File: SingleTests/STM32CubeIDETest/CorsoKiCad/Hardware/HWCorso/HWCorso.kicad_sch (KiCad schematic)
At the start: 9 parts

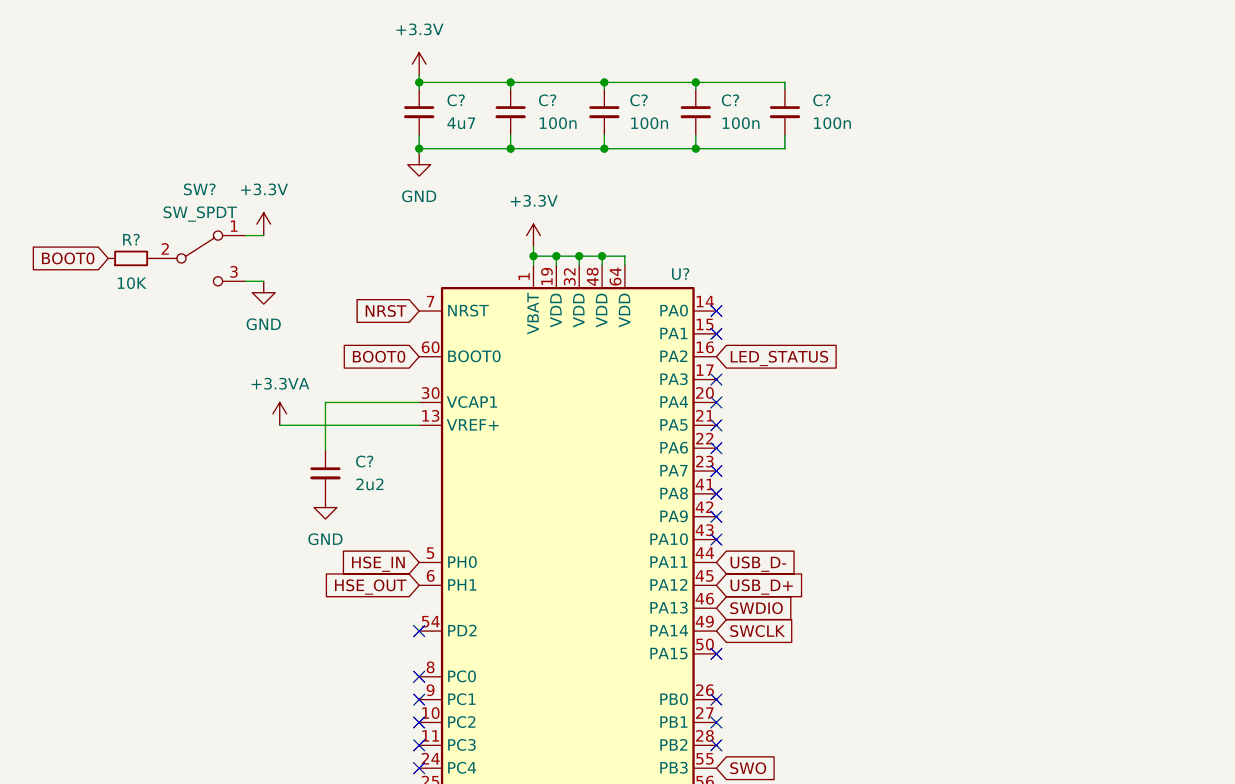
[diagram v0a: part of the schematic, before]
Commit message: Aggiunta dei filtri negli input e Cristallo
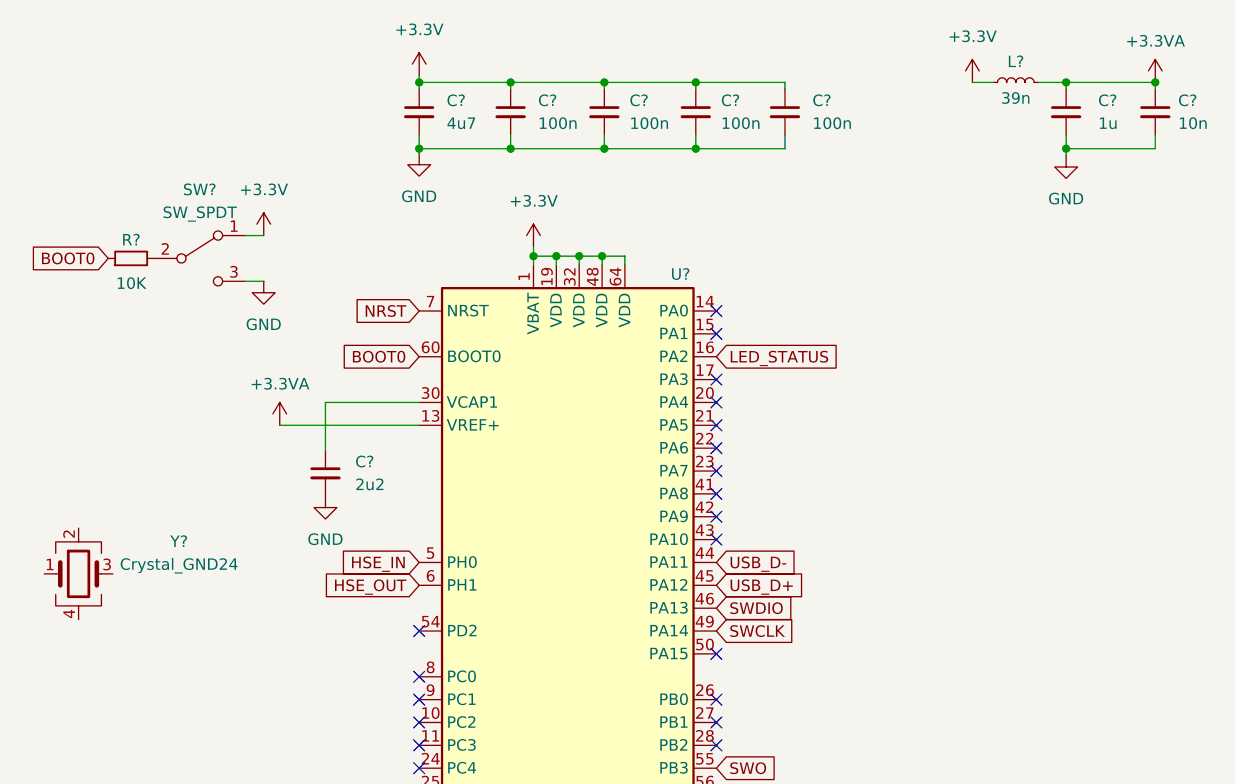
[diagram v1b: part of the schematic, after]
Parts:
- added C?: 10n, symbol Device:C_Small
- added C?: 1u, symbol Device:C_Small
- added L?: 39n, symbol Device:L_Small
- added Y?: Crystal_GND24, symbol Device:Crystal_GND24
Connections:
- net +3.3VA: now also C?.1, C?.1, L?.2
- net +3V3: now also L?.1
- net GND: now also C?.2, C?.2
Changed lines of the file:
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@@
     (company "Giovanni Rasera")
   )
+  (junction (at 133.604 71.882) (diameter 0) (color 0 0 0 0)
+  )
   (junction (at 92.456 71.882) (diameter 0) (color 0 0 0 0)
   )
+  (junction (at 133.604 79.248) (diameter 0) (color 0 0 0 0)
+  )
   (junction (at 82.296 71.882) (diameter 0) (color 0 0 0 0)
+  )
+  (junction (at 143.51 71.882) (diameter 0) (color 0 0 0 0)
   )
   (junction (at 71.882 79.248) (diameter 0) (color 0 0 0 0)
@@
     (stroke (width 0) (type default) (color 0 0 0 0))
   )
+  (wire (pts (xy 133.604 79.248) (xy 133.604 80.01))
+    (stroke (width 0) (type default) (color 0 0 0 0))
+  )
   (wire (pts (xy 79.502 181.102) (xy 79.502 182.372))
     (stroke (width 0) (type default) (color 0 0 0 0))
@@
     (stroke (width 0) (type default) (color 0 0 0 0))
   )
+  (wire (pts (xy 130.556 71.882) (xy 133.604 71.882))
+    (stroke (width 0) (type default) (color 0 0 0 0))
+  )
+  (wire (pts (xy 133.604 79.248) (xy 143.51 79.248))
+    (stroke (width 0) (type default) (color 0 0 0 0))
+  )
   (wire (pts (xy 92.456 77.724) (xy 92.456 79.248))
     (stroke (width 0) (type default) (color 0 0 0 0))
@@
     (stroke (width 0) (type default) (color 0 0 0 0))
   )
+  (wire (pts (xy 123.19 71.882) (xy 125.476 71.882))
+    (stroke (width 0) (type default) (color 0 0 0 0))
+  )
   (wire (pts (xy 92.456 72.644) (xy 92.456 71.882))
     (stroke (width 0) (type default) (color 0 0 0 0))
@@
     (stroke (width 0) (type default) (color 0 0 0 0))
   )
+  (wire (pts (xy 143.51 71.882) (xy 133.604 71.882))
+    (stroke (width 0) (type default) (color 0 0 0 0))
+  )
   (wire (pts (xy 71.882 79.248) (xy 71.882 77.724))
     (stroke (width 0) (type default) (color 0 0 0 0))
   )
+  (wire (pts (xy 143.51 79.248) (xy 143.51 77.724))
+    (stroke (width 0) (type default) (color 0 0 0 0))
+  )
   (wire (pts (xy 79.502 91.186) (xy 82.042 91.186))
     (stroke (width 0) (type default) (color 0 0 0 0))
@@
     (stroke (width 0) (type default) (color 0 0 0 0))
   )
+  (wire (pts (xy 133.604 77.724) (xy 133.604 79.248))
+    (stroke (width 0) (type default) (color 0 0 0 0))
+  )
+  (wire (pts (xy 143.51 72.644) (xy 143.51 71.882))
+    (stroke (width 0) (type default) (color 0 0 0 0))
+  )
   (wire (pts (xy 74.422 181.102) (xy 74.422 182.372))
     (stroke (width 0) (type default) (color 0 0 0 0))
@@
   )
   (wire (pts (xy 61.722 79.248) (xy 61.722 79.756))
+    (stroke (width 0) (type default) (color 0 0 0 0))
+  )
+  (wire (pts (xy 133.604 71.882) (xy 133.604 72.644))
     (stroke (width 0) (type default) (color 0 0 0 0))
   )
@@
       (effects (font (size 1.27 1.27)) (justify right) hide)
     )
+  )
+  (symbol (lib_id "Device:L_Small") (at 128.016 71.882 90) (unit 1)
+    (in_bom yes) (on_board yes)
+    (property "Reference" "L?" (id 0) (at 128.016 69.596 90))
+    (property "Value" "39n" (id 1) (at 128.016 73.66 90))
+    (property "Footprint" "" (id 2) (at 128.016 71.882 0)
+      (effects (font (size 1.27 1.27)) hide)
+    )
+    (property "Datasheet" "~" (id 3) (at 128.016 71.882 0)
+      (effects (font (size 1.27 1.27)) hide)
+    )
+    (pin "1")
+    (pin "2")
+  )
+  (symbol (lib_id "Device:C_Small") (at 143.51 75.184 0) (unit 1)
+    (in_bom yes) (on_board yes) (fields_autoplaced)
+    (property "Reference" "C?" (id 0) (at 146.05 73.9202 0)
+      (effects (font (size 1.27 1.27)) (justify left))
+    )
+    (property "Value" "10n" (id 1) (at 146.05 76.4602 0)
+      (effects (font (size 1.27 1.27)) (justify left))
+    )
+    (property "Footprint" "" (id 2) (at 143.51 75.184 0)
+      (effects (font (size 1.27 1.27)) hide)
+    )
+    (property "Datasheet" "~" (id 3) (at 143.51 75.184 0)
+      (effects (font (size 1.27 1.27)) hide)
+    )
+    (pin "1")
+    (pin "2")
   )
   (symbol (lib_id "Device:R_Small") (at 29.718 91.44 90) (unit 1)
@@
     (pin "1")
   )
+  (symbol (lib_id "Device:C_Small") (at 133.604 75.184 0) (unit 1)
+    (in_bom yes) (on_board yes) (fields_autoplaced)
+    (property "Reference" "C?" (id 0) (at 137.16 73.9202 0)
+      (effects (font (size 1.27 1.27)) (justify left))
+    )
+    (property "Value" "1u" (id 1) (at 137.16 76.4602 0)
+      (effects (font (size 1.27 1.27)) (justify left))
+    )
+    (property "Footprint" "" (id 2) (at 133.604 75.184 0)
+      (effects (font (size 1.27 1.27)) hide)
+    )
+    (property "Datasheet" "~" (id 3) (at 133.604 75.184 0)
+      (effects (font (size 1.27 1.27)) hide)
+    )
+    (pin "1")
+    (pin "2")
+  )
   (symbol (lib_id "Device:C_Small") (at 82.296 75.184 0) (unit 1)
     (in_bom yes) (on_board yes) (fields_autoplaced)
@@
     (pin "1")
     (pin "2")
+  )
+  (symbol (lib_id "power:GND") (at 133.604 80.01 0) (unit 1)
+    (in_bom yes) (on_board yes) (fields_autoplaced)
+    (property "Reference" "#PWR?" (id 0) (at 133.604 86.36 0)
+      (effects (font (size 1.27 1.27)) hide)
+    )
+    (property "Value" "GND" (id 1) (at 133.604 84.836 0))
+    (property "Footprint" "" (id 2) (at 133.604 80.01 0)
+      (effects (font (size 1.27 1.27)) hide)
+    )
+    (property "Datasheet" "" (id 3) (at 133.604 80.01 0)
+      (effects (font (size 1.27 1.27)) hide)
+    )
+    (pin "1")
+  )
+  (symbol (lib_id "power:+3.3VA") (at 143.51 71.882 0) (unit 1)
+    (in_bom yes) (on_board yes) (fields_autoplaced)
+    (property "Reference" "#PWR?" (id 0) (at 143.51 75.692 0)
+      (effects (font (size 1.27 1.27)) hide)
+    )
+    (property "Value" "+3.3VA" (id 1) (at 143.51 67.31 0))
+    (property "Footprint" "" (id 2) (at 143.51 71.882 0)
+      (effects (font (size 1.27 1.27)) hide)
+    )
+    (property "Datasheet" "" (id 3) (at 143.51 71.882 0)
+      (effects (font (size 1.27 1.27)) hide)
+    )
+    (pin "1")
+  )
+  (symbol (lib_id "power:+3.3V") (at 123.19 71.882 0) (unit 1)
+    (in_bom yes) (on_board yes) (fields_autoplaced)
+    (property "Reference" "#PWR?" (id 0) (at 123.19 75.692 0)
+      (effects (font (size 1.27 1.27)) hide)
+    )
+    (property "Value" "+3.3V" (id 1) (at 123.19 66.802 0))
+    (property "Footprint" "" (id 2) (at 123.19 71.882 0)
+      (effects (font (size 1.27 1.27)) hide)
+    )
+    (property "Datasheet" "" (id 3) (at 123.19 71.882 0)
+      (effects (font (size 1.27 1.27)) hide)
+    )
+    (pin "1")
   )
   (symbol (lib_id "power:GND") (at 51.308 117.856 0) (unit 1)
@@
     (pin "1")
   )
+  (symbol (lib_id "Device:Crystal_GND24") (at 23.876 126.492 0) (unit 1)
+    (in_bom yes) (on_board yes) (fields_autoplaced)
+    (property "Reference" "Y?" (id 0) (at 35.052 122.9106 0))
+    (property "Value" "Crystal_GND24" (id 1) (at 35.052 125.4506 0))
+    (property "Footprint" "" (id 2) (at 23.876 126.492 0)
+      (effects (font (size 1.27 1.27)) hide)
+    )
+    (property "Datasheet" "~" (id 3) (at 23.876 126.492 0)
+      (effects (font (size 1.27 1.27)) hide)
+    )
+    (pin "1")
+    (pin "2")
+    (pin "3")
+    (pin "4")
+  )
   (symbol (lib_id "Switch:SW_SPDT") (at 37.338 91.44 0) (unit 1)
     (in_bom yes) (on_board yes) (fields_autoplaced)
@@
       (reference "#PWR?") (unit 1) (value "+3.3V") (footprint "")
     )
+    (path "/6ec52dc9-9aec-4bf2-9fd3-c0cd46b729c7"
+      (reference "#PWR?") (unit 1) (value "GND") (footprint "")
+    )
+    (path "/7a704518-be5b-4a5d-8c91-6557660f7c8c"
+      (reference "#PWR?") (unit 1) (value "+3.3VA") (footprint "")
+    )
+    (path "/80973bb3-f981-4563-90cd-8e6f3f7690f9"
+      (reference "#PWR?") (unit 1) (value "+3.3V") (footprint "")
+    )
     (path "/858621a7-61c6-406a-9565-f0db88deaafb"
       (reference "#PWR?") (unit 1) (value "GND") (footprint "")
@@
       (reference "#PWR?") (unit 1) (value "GND") (footprint "")
     )
+    (path "/0b4bde23-a6f7-43ef-b274-a7947ddde5c0"
+      (reference "C?") (unit 1) (value "10n") (footprint "")
+    )
     (path "/1787e3ec-0a42-4bb9-9c62-69d81f2faa0c"
       (reference "C?") (unit 1) (value "100n") (footprint "")
     )
+    (path "/3ecf98df-3964-489a-bf42-83d2ab05a7a6"
+      (reference "C?") (unit 1) (value "1u") (footprint "")
+    )
     (path "/42c6cb80-7344-4e57-8989-b8d2ce8c323a"
       (reference "C?") (unit 1) (value "100n") (footprint "")
@@
       (reference "C?") (unit 1) (value "100n") (footprint "")
     )
+    (path "/012e7db6-df96-4dd9-9ade-dc468d8e322c"
+      (reference "L?") (unit 1) (value "39n") (footprint "")
+    )
     (path "/10ed8720-e1d5-4960-9773-9cedaefe4acc"
       (reference "R?") (unit 1) (value "10K") (footprint "")
@@
       (reference "U?") (unit 1) (value "STM32F401RCT6") (footprint "Package_QFP:LQFP-64_10x10mm_P0.5mm")
     )
-  )
+    (path "/ad4f76c5-6da7-44a3-8a24-99f0e3e61fba"
+      (reference "Y?") (unit 1) (value "Crystal_GND24") (footprint "")
+    )
+  )

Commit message: Creazione della scheda del flight controller
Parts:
- added C? (x2): 12p, symbol Device:C_Small
- added C?: 10n, symbol Device:C_Small
- added C?: 4u7, symbol Device:C_Small
- added C?: 22u, symbol Device:C_Small
- added D?: B5819W, symbol Device:D_Schottky_Small
- added D?: BLUE, symbol Device:LED_Small
- added F?: 250mA, symbol Device:Polyfuse_Small
- added FB?: 600 @ 600MHz, symbol Device:FerriteBead_Small
- added L?: 10u, symbol Device:L_Small
- added Q?: AO3401A, Package_TO_SOT_SMD:SOT-23, symbol Transistor_FET:AO3401A
- added R?: 15K, symbol Device:R_Small
- added R?: 47K, symbol Device:R_Small
- added R?: 100K, symbol Device:R_Small
- added R?: 1K5, symbol Device:R_Small
- added R?: 47, symbol Device:R_Small
- added R?: 270, symbol Device:R_Small
- added R?: 68K, symbol Device:R_Small
- added U?: MP2359DJ-LF-Z, symbol Converter_DCDC:MP2359DJ-LF-Z
- Y?: value Crystal_GND24 -> 16MHz
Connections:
- net +3V3: now also C?.2, L?.2, R?.2
- net GND: now also Y?.2, Y?.4, C?.1, C?.2, C?.2, C?.2, D?.2 (A), Q?.1 (G), R?.1, R?.1, R?.1, U?.2 (GND)
- net HSE_IN: now also Y?.1, C?.1
- net HSE_OUT: now also R?.1
- net LED_STATUS: now also D?.2 (A)
- net at Y?.3: now also C?.1, R?.2
- new net: R?.1, R?.2
- new net: D?.1 (K), R?.2
- new net: FB?.1, Q?.2 (S)
- new net: F?.2, Q?.3 (D)
- new net +12V: F?.1
- new net BUCK_BST: C?.1, U?.1 (BST)
- new net BUCK_EN: R?.1, R?.2, U?.4 (EN)
- new net BUCK_FB: R?.1, R?.2, U?.3 (FB)
- new net BUCK_IN: C?.1, FB?.2, R?.2, U?.5 (IN)
- new net BUCK_SW: C?.2, D?.1 (K), L?.1, U?.6 (SW)
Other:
- note added: "Capacitor as in the datasheet of the Regulator"
- note added: "Enable PIN needs a stepdown"
- note added: "MCU"
- note added: "POWER"
- note added: "Reverse polarity protection"
- moved on the sheet: C?, L?, R?, SW?, U?, Y?

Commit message: Scelta componenti e creazione PCD
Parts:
- added D2: B5819W, Diode_SMD:D_SOD-123, symbol Device:D_Schottky_Small
- added D4: RED, LED_SMD:LED_0603_1608Metric, symbol Device:LED_Small
- added H1, H2, H3, H4: MountingHole_Pad, MountingHole:MountingHole_4.3mm_M4_Pad_Via, symbol Mechanical:MountingHole_Pad
- added J1: USB_B_Mini, Connector_USB:USB_Mini-B_Wuerth_65100516121_Horizontal, symbol Connector:USB_B_Mini
- added J2: BATTERY, TerminalBlock_Phoenix:TerminalBlock_Phoenix_PT-1,5-2-3.5-H_1x02_P3.50mm_Horizontal, symbol Connector:Screw_Terminal_01x02
- added J3: I2C_CONN, Connector_Molex:Molex_PicoBlade_53048-0410_1x04_P1.25mm_Horizontal, symbol Connector_Generic:Conn_01x04
- added J4: SWD_CONN, Connector_PinSocket_1.27mm:PinSocket_2x05_P1.27mm_Vertical_SMD, symbol Connector_Generic:Conn_02x05_Odd_Even
- added J5: USART6_CONN, Connector_Molex:Molex_PicoBlade_53048-0410_1x04_P1.25mm_Horizontal, symbol Connector_Generic:Conn_01x04
- added R11: 1K, Resistor_SMD:R_0603_1608Metric, symbol Device:R_Small
- added R5, R7: 2k2, Resistor_SMD:R_0603_1608Metric, symbol Device:R_Small
- added U3: USBLC6-2SC6, Package_TO_SOT_SMD:SOT-23-6, symbol Power_Protection:USBLC6-2SC6
- C1, C10, C12, C2: renamed from C?; footprint (none) -> Capacitor_SMD:C_0603_1608Metric
- C11, C3, C4, C5, C7, C8, C9: renamed from C?; footprint (none) -> Capacitor_SMD:C_0402_1005Metric
- C13: renamed from C?; footprint (none) -> Capacitor_SMD:C_1206_3216Metric
- C6: renamed from C?; value 4u7 -> 10U; footprint (none) -> Capacitor_SMD:C_1206_3216Metric
- D1: renamed from D?; footprint (none) -> LED_SMD:LED_0603_1608Metric
- D3: renamed from D?; footprint (none) -> Diode_SMD:D_SOD-123
- F1: renamed from F?; footprint (none) -> Fuse:Fuse_0603_1608Metric
- FB1: renamed from FB?; footprint (none) -> Inductor_SMD:L_0805_2012Metric
- L1: renamed from L?; footprint (none) -> Inductor_SMD:L_0402_1005Metric
- L2: renamed from L?; footprint (none) -> Inductor_SMD:L_Sunlord_MWSA0518_5.4x5.2mm
- R1, R10, R2, R3, R8, R9: renamed from R?; footprint (none) -> Resistor_SMD:R_0603_1608Metric
- R4, R6: renamed from R?; footprint (none) -> Resistor_SMD:R_0402_1005Metric
- SW1: renamed from SW?; footprint (none) -> Button_Switch_SMD:SW_SPDT_PCM12
- U2: renamed from U?; footprint (none) -> Package_TO_SOT_SMD:SOT-23-6
- Y1: renamed from Y?; footprint (none) -> Crystal:Crystal_SMD_3225-4Pin_3.2x2.5mm
- gave numbers to parts that had none: 2
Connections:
- net +12V: now also J2.1 (Pin_1)
- net +3V3: now also D4.2 (A), J3.1 (Pin_1), J4.1 (Pin_1), J5.1 (Pin_1), R5.1, R7.1
- net GND: now also H1.1, H2.1, H3.1, H4.1, J1.5 (GND), J2.2 (Pin_2), J3.4 (Pin_4), J4.3 (Pin_3), J4.5 (Pin_5), J4.9 (Pin_9), J5.4 (Pin_4), R11.1, U3.2 (GND)
- net I2C1_SCL: now also J3.2 (Pin_2), R5.2
- net I2C1_SDA: now also J3.3 (Pin_3), R7.2
- net NRST: now also J4.10 (Pin_10)
- net SWCLK: now also J4.4 (Pin_4)
- net SWDIO: now also J4.2 (Pin_2)
- net SWO: now also J4.6 (Pin_6)
- net USART6_RX: now also J5.3 (Pin_3)
- net USART6_TX: now also J5.2 (Pin_2)
- net USB_D+: now also U3.4 (I/O2)
- net USB_D-: now also U3.6 (I/O1)
- net at FB1.1, Q1.2 (S): now also D2.1 (K)
- new net: D4.1 (K), R11.2
- new net +5V: D2.2 (A), J1.1 (VBUS), U3.5 (VBUS)
- new net USB_CONN_D+: J1.3 (D+), U3.3 (I/O2)
- new net USB_CONN_D-: J1.2 (D-), U3.1 (I/O1)
- no-connect marks 38 -> 42
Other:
- note added: "CONNECTIVITY"
- note added: "I2C / USART"
- note added: "POWER / DEBUG"
- note added: "USB"
- moved on the sheet: C11, C12, C13, C6, C9, D3, FB1, L2, R10, R2, R3, R6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

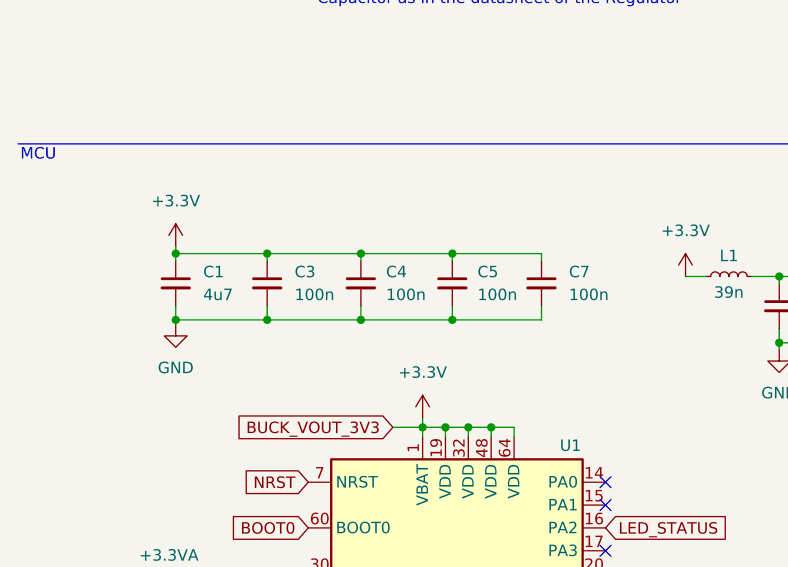
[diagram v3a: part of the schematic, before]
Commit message: Posizionamento dei componenti
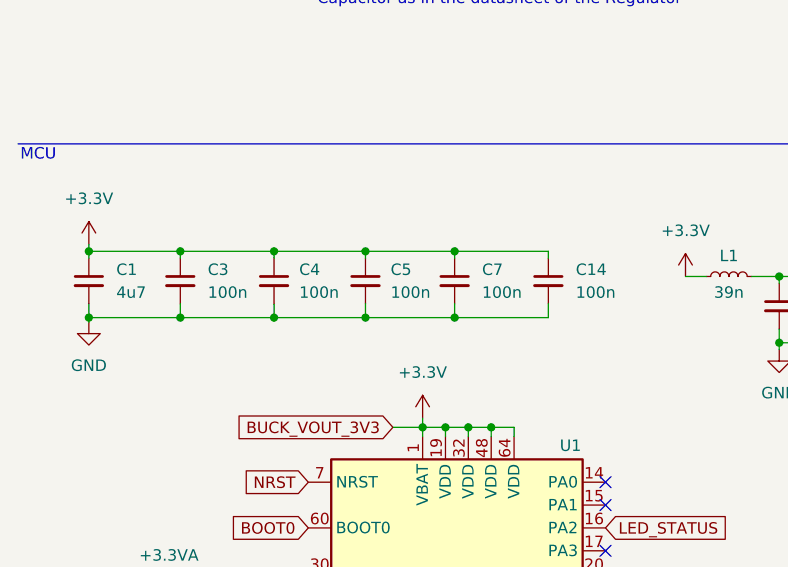
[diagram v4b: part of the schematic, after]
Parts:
- added C14: 100n, Capacitor_SMD:C_0402_1005Metric, symbol Device:C_Small
- C10: footprint Capacitor_SMD:C_0603_1608Metric -> Capacitor_SMD:C_0402_1005Metric
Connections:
- net +3V3: now also C14.1
- net GND: now also C14.2
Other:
- moved on the sheet: C1, C3, C4, C5, C7

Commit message: Layout della scheda
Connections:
- net +12V: now also Q1.3 (D); no longer F1.1
- net at D2.1 (K), Q1.2 (S): now also F1.1; no longer FB1.1
- net at F1.2: now also FB1.1; no longer Q1.3 (D)
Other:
- moved on the sheet: C6, D2, F1, FB1, Q1

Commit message: Routing della scheda
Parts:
- J4: footprint Connector_PinSocket_1.27mm:PinSocket_2x05_P1.27mm_Vertical_SMD -> Connector_PinHeader_1.27mm:PinHeader_2x05_P1.27mm_Vertical_SMD
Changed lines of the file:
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@@
     (property "Reference" "J4" (id 0) (at 216.662 70.612 0))
     (property "Value" "SWD_CONN" (id 1) (at 216.916 87.884 0))
-    (property "Footprint" "Connector_PinSocket_1.27mm:PinSocket_2x05_P1.27mm_Vertical_SMD" (id 2) (at 215.392 78.486 0)
+    (property "Footprint" "Connector_PinHeader_1.27mm:PinHeader_2x05_P1.27mm_Vertical_SMD" (id 2) (at 215.392 78.486 0)
       (effects (font (size 1.27 1.27)) hide)
     )
@@
     )
     (path "/2a63d06b-6465-4f67-a91b-0d27b5ae0d4f"
-      (reference "J4") (unit 1) (value "SWD_CONN") (footprint "Connector_PinSocket_1.27mm:PinSocket_2x05_P1.27mm_Vertical_SMD")
+      (reference "J4") (unit 1) (value "SWD_CONN") (footprint "Connector_PinHeader_1.27mm:PinHeader_2x05_P1.27mm_Vertical_SMD")
     )
     (path "/fc3aa937-a42c-45b5-b421-c4e0cc21ed87"

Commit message: File BOM e traduzione del file XML in csv
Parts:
- C1: LCSC Part # (none) -> C19666
- C10: LCSC Part # (none) -> C15195
- C11, C9: LCSC Part # (none) -> C1547
- C12: LCSC Part # (none) -> C57112
- C13: LCSC Part # (none) -> C12891
- C14, C3, C4, C5, C7: LCSC Part # (none) -> C307331
- C2: LCSC Part # (none) -> C23630
- C6: LCSC Part # (none) -> C13585
- C8: LCSC Part # (none) -> C52923
- D1: LCSC Part # (none) -> C72041
- D2, D3: LCSC Part # (none) -> C8598
- D4: LCSC Part # (none) -> C2286
- F1: LCSC Part # (none) -> C151137
- FB1: LCSC Part # (none) -> C1017
- L1: LCSC Part # (none) -> C26443
- L2: LCSC Part # (none) -> C139506
- Q1: LCSC Part # (none) -> C15127
- R1: LCSC Part # (none) -> C22843
- R10: LCSC Part # (none) -> C22966
- R11: LCSC Part # (none) -> C21190
- R2: LCSC Part # (none) -> C25803
- R3: LCSC Part # (none) -> C23231
- R4: LCSC Part # (none) -> C25744
- R5, R7: LCSC Part # (none) -> C4190
- R6: LCSC Part # (none) -> C25792
- R8: LCSC Part # (none) -> C25819
- R9: LCSC Part # (none) -> C22809
- U1: LCSC Part # (none) -> C74524
- U2: LCSC Part # (none) -> C14259
- U3: LCSC Part # (none) -> C2827654
- Y1: LCSC Part # (none) -> C13738
